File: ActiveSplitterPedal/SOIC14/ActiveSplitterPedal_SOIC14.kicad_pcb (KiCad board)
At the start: 2 copper layers, 124 x 100.8 mm, 57 parts, among them J1 MonoJack2Switch, J2 MonoJack2Switch, J3 MonoJack2Switch, J4 MonoJack2Switch, J5 MonoJack2Switch, J6 Barrel_Jack, U1 TL074, U10 TPS60400, U2 TL074, U3 TL074, U4 TL074, U9 SE8250X2

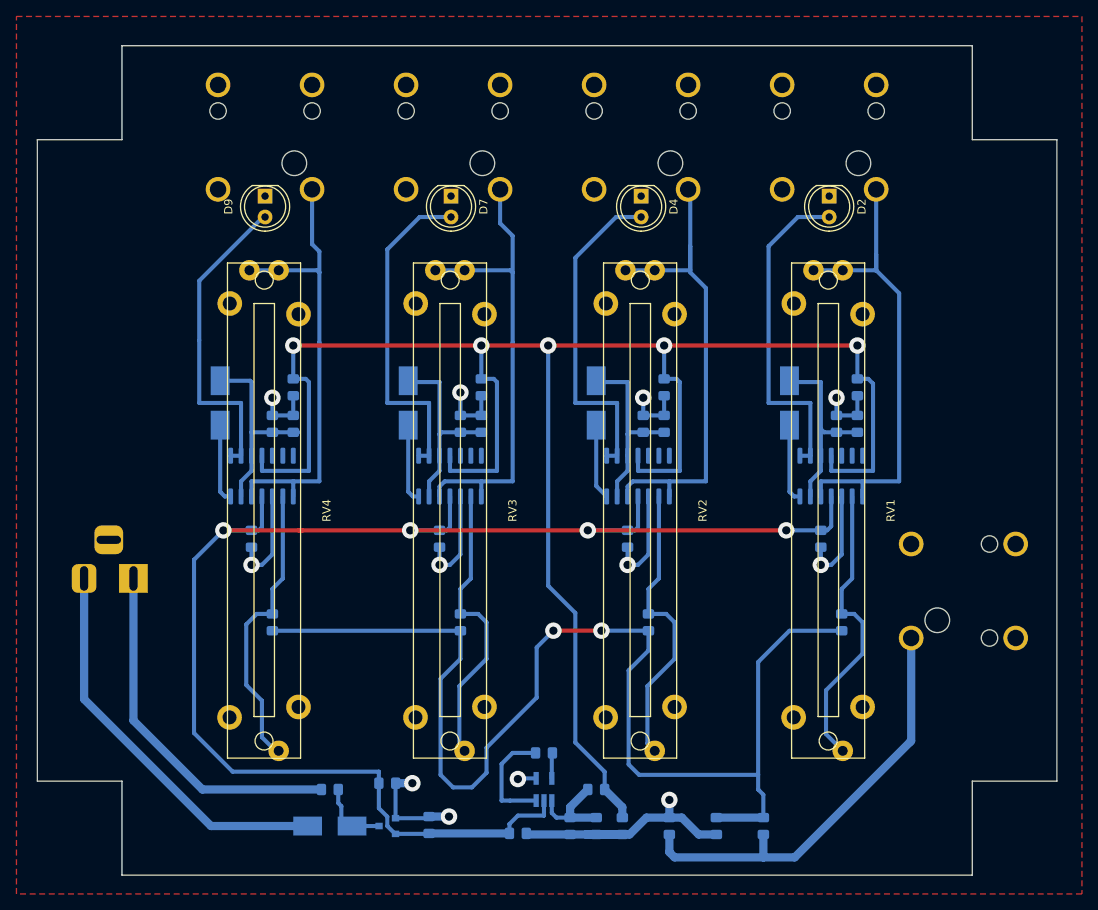
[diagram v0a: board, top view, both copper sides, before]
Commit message: RevA HW updates
- Replaced SW Diode with Schottky Diode
- Added one charge pump IC per quad opamp (60mA each)
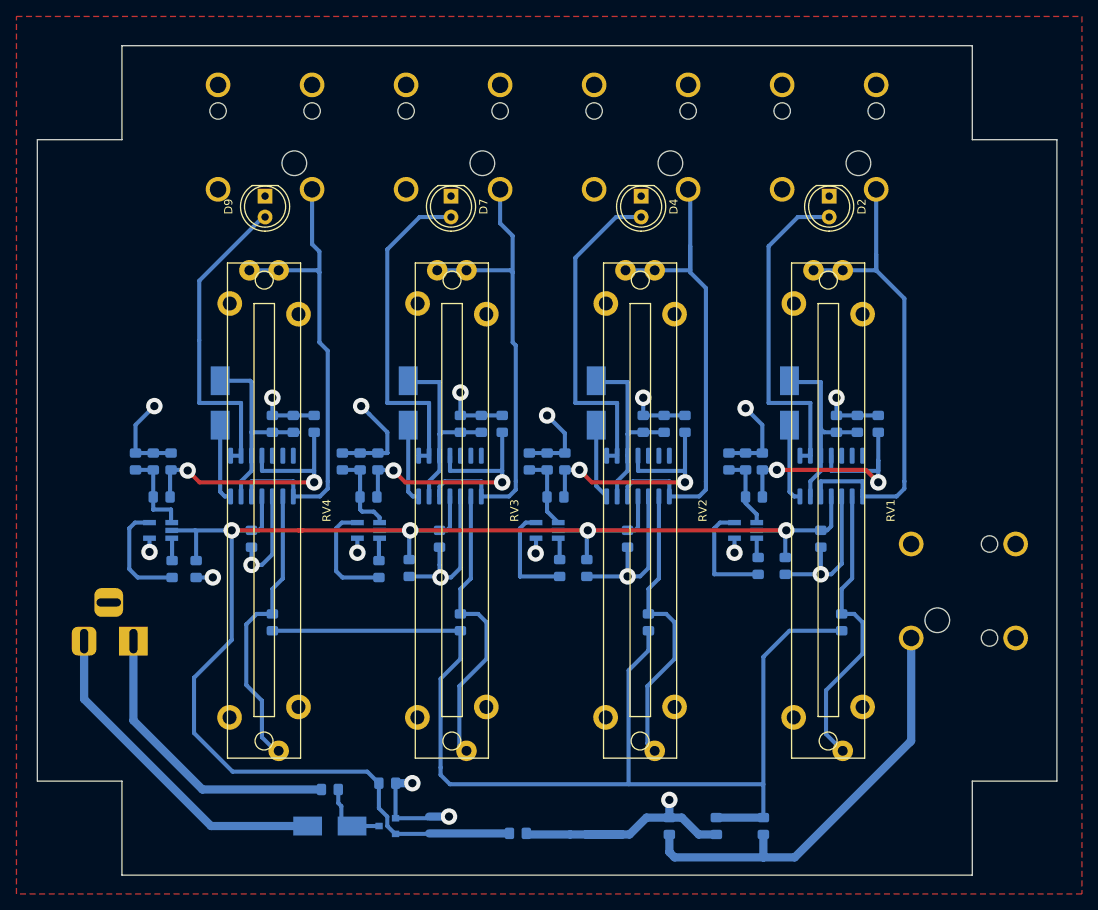
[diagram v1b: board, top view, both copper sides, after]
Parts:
- removed U10: TPS60400, Package_TO_SOT_SMD:SOT-23-5_HandSoldering
- added C21: 1uF, Capacitor_SMD:C_0805_2012Metric_Pad1.15x1.40mm_HandSolder, B.Cu at (184.9, 87.4)
- added C22: 1uF, Capacitor_SMD:C_0805_2012Metric_Pad1.15x1.40mm_HandSolder, B.Cu at (181.2, 87.5)
- added C23: 1uF, Capacitor_SMD:C_0805_2012Metric_Pad1.15x1.40mm_HandSolder, B.Cu at (176.8, 74.4)
- added C24: 1uF, Capacitor_SMD:C_0805_2012Metric_Pad1.15x1.40mm_HandSolder, B.Cu at (181.1, 74.4)
- added C25: 1uF, Capacitor_SMD:C_0805_2012Metric_Pad1.15x1.40mm_HandSolder, B.Cu at (159.0, 87.5)
- added C26: 1uF, Capacitor_SMD:C_0805_2012Metric_Pad1.15x1.40mm_HandSolder, B.Cu at (156.1, 87.5)
- added C27: 1uF, Capacitor_SMD:C_0805_2012Metric_Pad1.15x1.40mm_HandSolder, B.Cu at (153.8, 74.4)
- added C28: 1uF, Capacitor_SMD:C_0805_2012Metric_Pad1.15x1.40mm_HandSolder, B.Cu at (156.0, 74.4)
- added C29: 1uF, Capacitor_SMD:C_0805_2012Metric_Pad1.15x1.40mm_HandSolder, B.Cu at (230.6, 87.1)
- added C30: 1uF, Capacitor_SMD:C_0805_2012Metric_Pad1.15x1.40mm_HandSolder, B.Cu at (227.3, 87.1)
- added C31: 1uF, Capacitor_SMD:C_0805_2012Metric_Pad1.15x1.40mm_HandSolder, B.Cu at (223.8, 74.4)
- added C32: 1uF, Capacitor_SMD:C_0805_2012Metric_Pad1.15x1.40mm_HandSolder, B.Cu at (227.8, 74.4)
- added C33: 100nF, Capacitor_SMD:C_0805_2012Metric_Pad1.15x1.40mm_HandSolder, B.Cu at (178.9, 74.4)
- added C34: 100nF, Capacitor_SMD:C_0805_2012Metric_Pad1.15x1.40mm_HandSolder, B.Cu at (151.6, 74.4)
- added C35: 100nF, Capacitor_SMD:C_0805_2012Metric_Pad1.15x1.40mm_HandSolder, B.Cu at (225.8, 74.4)
- added R13: 100R, Resistor_SMD:R_0805_2012Metric_Pad1.15x1.40mm_HandSolder, B.Cu at (180.0, 78.7)
- added R14: 100R, Resistor_SMD:R_0805_2012Metric_Pad1.15x1.40mm_HandSolder, B.Cu at (154.8, 78.7)
- added R15: 100R, Resistor_SMD:R_0805_2012Metric_Pad1.15x1.40mm_HandSolder, B.Cu at (226.8, 78.7)
- added U5: TPS60400, Package_TO_SOT_SMD:SOT-23-5_HandSoldering, B.Cu at (201.7, 82.8)
- added U6: TPS60400, Package_TO_SOT_SMD:SOT-23-5_HandSoldering, B.Cu at (180.0, 82.8)
- added U7: TPS60400, Package_TO_SOT_SMD:SOT-23-5_HandSoldering, B.Cu at (154.7, 82.8)
- added U8: TPS60400, Package_TO_SOT_SMD:SOT-23-5_HandSoldering, B.Cu at (225.8, 82.8)
- D1, D3, D6, D8: value 1N914 -> D_Schottky
- moved D8 69.2 mm to (231.1, 67.3)
- moved C3 45.1 mm to (199.5, 74.4), turned to 90 degrees
- moved C11 44.9 mm to (203.8, 74.4), turned to 90 degrees
- moved C9 44.4 mm to (201.7, 74.4), turned to 90 degrees
- moved C1 36.7 mm to (206.5, 87.4), turned to 270 degrees
- moved R8 35.9 mm to (202.7, 78.7)
- moved D1 23.5 mm to (207.6, 67.3)
- moved D3 22.9 mm to (184.8, 67.3)
- moved D6 22.9 mm to (161.9, 67.3)
- moved C2 22.6 mm to (203.2, 87.4), turned to 270 degrees
- moved J6 7.62 mm to (151.4, 96.3)
- moved C13 5.12 mm to (218.4, 69.8), turned to 90 degrees
- moved C16 5.12 mm to (196.2, 69.8), turned to 90 degrees
- moved C19 5.12 mm to (173.4, 69.8), turned to 90 degrees
- moved C6 5.12 mm to (241.9, 69.8), turned to 90 degrees
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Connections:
- net /PowerSupply/-5VOUT renamed /GainAndPeakDetector2/-5VOUT
- C11 pad 1: -5V -> /GainAndPeakDetector2/-5V_POL
- C13 pad 1: -5V -> /GainAndPeakDetector2/-5V_POL
- C16 pad 1: -5V -> /GainAndPeakDetector3/-5V_POL
- C19 pad 1: -5V -> /GainAndPeakDetector4/-5V_POL
- C6 pad 1: -5V -> /GainAndPeakDetector1/-5V_POL
- D1 pad 1: Net-(C7-Pad1) -> Net-(C14-Pad1)
- D3 pad 1: Net-(C14-Pad1) -> Net-(C17-Pad1)
- D6 pad 1: Net-(C17-Pad1) -> Net-(C20-Pad1)
- D8 pad 1: Net-(C20-Pad1) -> Net-(C7-Pad1)
- R8 pad 2: -5V -> /GainAndPeakDetector2/-5V_POL
- U1 pad 11: -5V -> /GainAndPeakDetector1/-5V_POL
- U1 pad 7: Net-(D1-Pad2) -> Net-(D8-Pad2)
- U2 pad 11: -5V -> /GainAndPeakDetector2/-5V_POL
- U2 pad 7: Net-(D3-Pad2) -> Net-(D1-Pad2)
- U3 pad 11: -5V -> /GainAndPeakDetector3/-5V_POL
- U3 pad 7: Net-(D6-Pad2) -> Net-(D3-Pad2)
- U4 pad 11: -5V -> /GainAndPeakDetector4/-5V_POL
- U4 pad 7: Net-(D8-Pad2) -> Net-(D6-Pad2)
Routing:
- net -5V: track 226.1 -> 0.00 mm, vias 5 -> 0
- net GNDS: track 167.8 -> 233.9 mm, vias 12 -> 20
- net /GainAndPeakDetector4/-5V_POL: track 0.00 -> 35.7 mm, vias 0 -> 2
- net /GainAndPeakDetector3/-5V_POL: track 0.00 -> 33.4 mm, vias 0 -> 2
- net /GainAndPeakDetector1/-5V_POL: track 0.00 -> 32.9 mm, vias 0 -> 2
- net /GainAndPeakDetector2/-5V_POL: track 0.00 -> 32.2 mm, vias 0 -> 2
- net +5V: track 186.3 -> 208.7 mm
- net /GainAndPeakDetector1/SIGNAL_INPUT: track 150.7 -> 136.7 mm, vias 2 -> 0
- net Net-(C30-Pad2): track 0.00 -> 13.7 mm
- net Net-(C22-Pad2): track 0.00 -> 13.6 mm
- net Net-(C26-Pad2): track 0.00 -> 13.3 mm
- net Net-(C2-Pad1): track 13.5 -> 2.67 mm
- net /GainAndPeakDetector4/-5VOUT: track 0.00 -> 10.8 mm
- net /GainAndPeakDetector3/-5VOUT: track 0.00 -> 10.4 mm
- net Net-(C2-Pad2): track 3.13 -> 12.9 mm
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
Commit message: Updated RevA layout
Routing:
- net /PowerSupply/+9V_IN: vias 0 -> 1
